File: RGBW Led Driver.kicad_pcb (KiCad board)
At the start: 2 copper layers, 66 x 50.8 mm, 23 parts, among them J1 Screw_Terminal_01x06, Q1 IRLZ44N, Q2 IRLZ44N, Q3 IRLZ44N, Q4 IRLZ44N, U1 TC4427xOA, U2 TC4427xOA

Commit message: Re-added autodeleted duplicate tracks
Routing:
- net 5v: track 124.2 -> 178.6 mm
- net GND_OUT1: track 20.5 -> 41.0 mm
- net GND: track 295.9 -> 314.3 mm
- net GND_OUT2: track 13.3 -> 26.6 mm
- net GND_OUT4: track 12.3 -> 24.5 mm
- net GND_OUT3: track 11.2 -> 22.4 mm

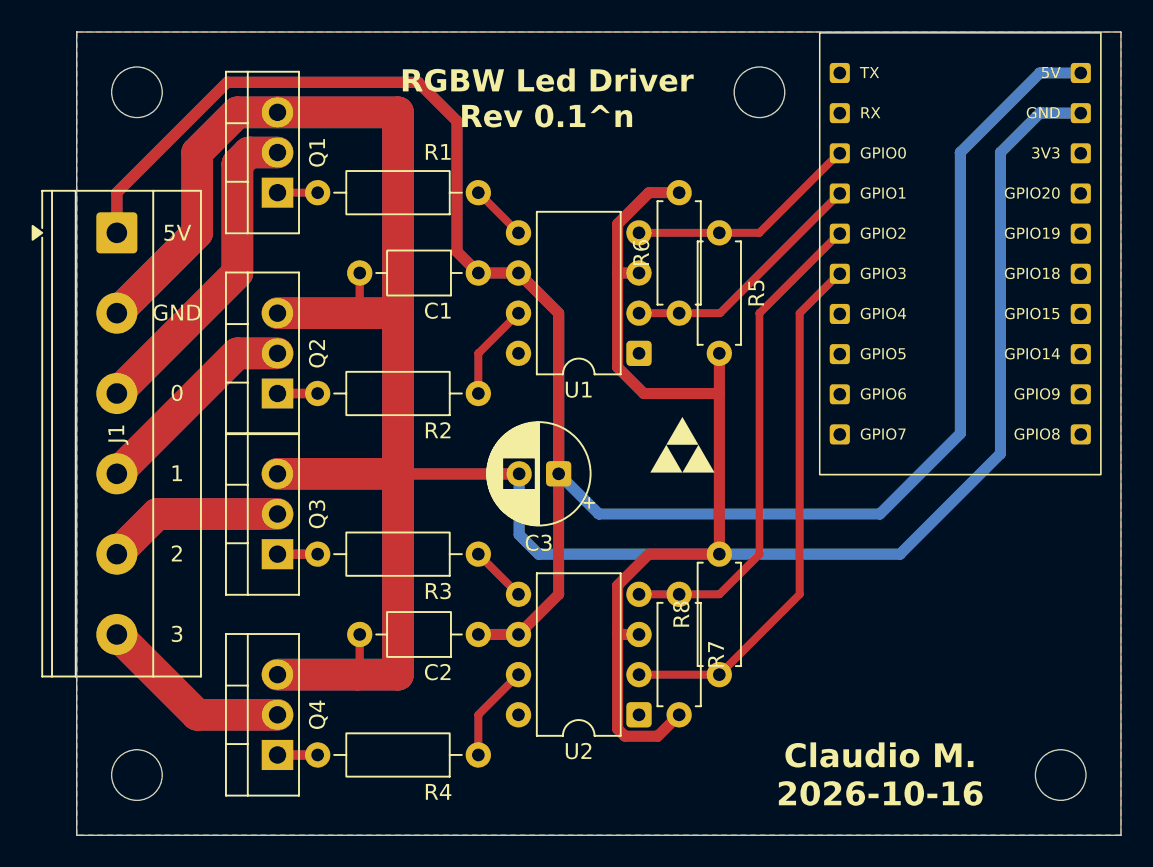
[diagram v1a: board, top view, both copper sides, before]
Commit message: Changed resistors footprint to smaller ones that i own
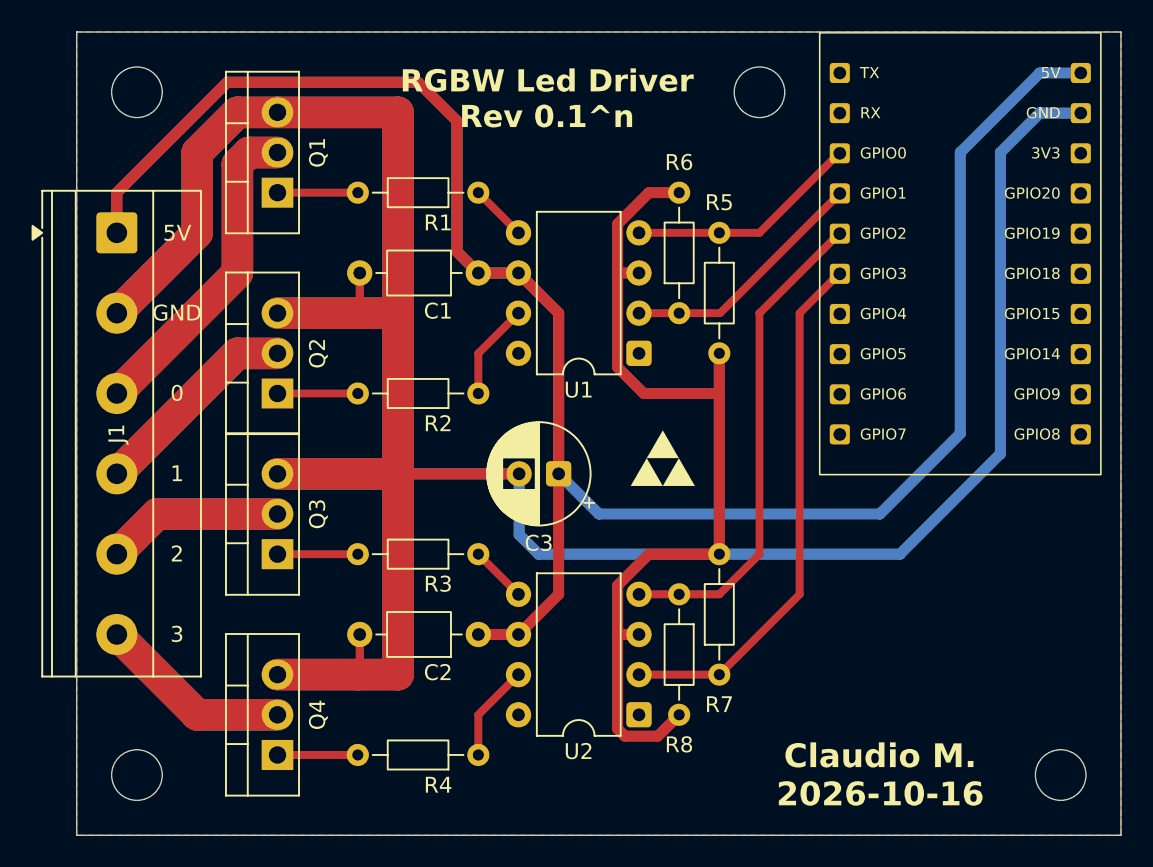
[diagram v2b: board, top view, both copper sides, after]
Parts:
- R1, R2, R3, R4: footprint Resistor_THT:R_Axial_DIN0207_L6.3mm_D2.5mm_P10.16mm_Horizontal -> Resistor_THT:R_Axial_DIN0204_L3.6mm_D1.6mm_P7.62mm_Horizontal
- R5, R6, R7, R8: footprint Resistor_THT:R_Axial_DIN0207_L6.3mm_D2.5mm_P7.62mm_Horizontal -> Resistor_THT:R_Axial_DIN0204_L3.6mm_D1.6mm_P7.62mm_Horizontal
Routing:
- net Net-(Q4-G): track 2.54 -> 5.08 mm
- net Net-(Q3-G): track 2.54 -> 5.08 mm
- net Net-(Q2-G): track 2.54 -> 5.08 mm
- net Net-(Q1-G): track 2.54 -> 5.08 mm
